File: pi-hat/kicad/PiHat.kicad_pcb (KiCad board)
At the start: 2 copper layers, 49.8 x 62 mm, 14 parts, among them J1 Raspberry_Pi_2_3, J2 Power, J3 HDMI board, J4 Fan, J5 CNC, J6 IDC16, J7 UVPanel, J8 Pro Power, Q1 BD139, U1 AMZ_3A_MOD

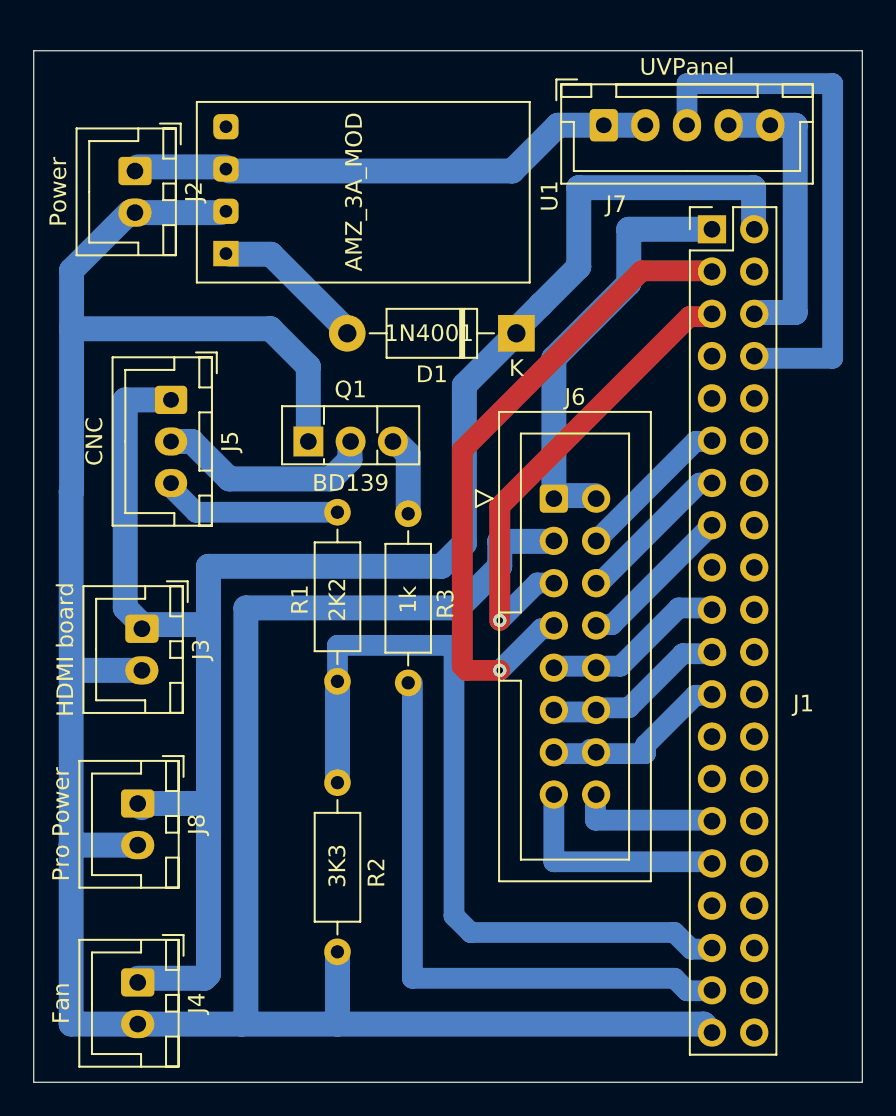
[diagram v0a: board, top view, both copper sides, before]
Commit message: PiHat Rev 2.1
Fix UV lamp ground thru GPIOs. Added buzzer trace.
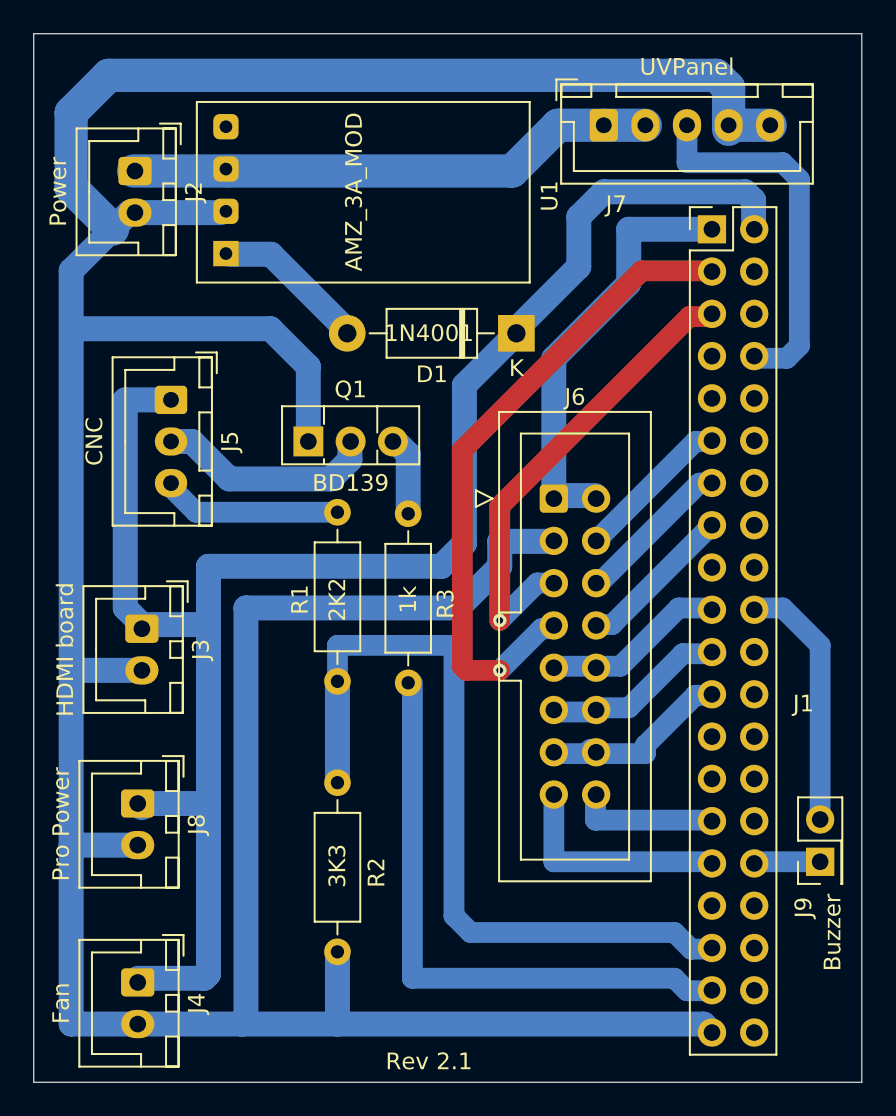
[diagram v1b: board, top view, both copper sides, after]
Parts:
- added J9: Buzzer, Connector_PinHeader_2.54mm:PinHeader_2x01_P2.54mm_Vertical, F.Cu at (57.4, 58.9)
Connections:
- J1 pad 20: Net-(J1-Pad20) -> GND
- J1 pad 32: Net-(J1-Pad32) -> Buzzer
- J1 pad 6: GND -> Net-(J1-Pad6)
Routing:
- net GND: track 189.6 -> 240.8 mm
- net UVControl: track 32.5 -> 22.5 mm
- net Buzzer: track 0.00 -> 4.00 mm
- net +5V: track 106.7 -> 105.6 mm
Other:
- board size 49.8 x 62 mm -> 49.8 x 63 mm
- board text added: "Rev 2.1"
